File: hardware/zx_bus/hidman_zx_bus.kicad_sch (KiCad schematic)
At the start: 42 parts, among them J1 X1A, J1 ZX Keyboard, J2 GOTEK, J2 X1B, J3 UART, J4 USB_A, J5 USB_A, J6 Keyboard, J7 JTAG, J7 Mouse, J8 Kempston Mouse, J9 Z80, SW1 RESET, SW2 BOOT0, SW3 BOOT1, U1 CH559L, U2 EPM3128ATC100, U3 AMS1117-3.3, U4 74LVC1G125DB, Y1 12MHz

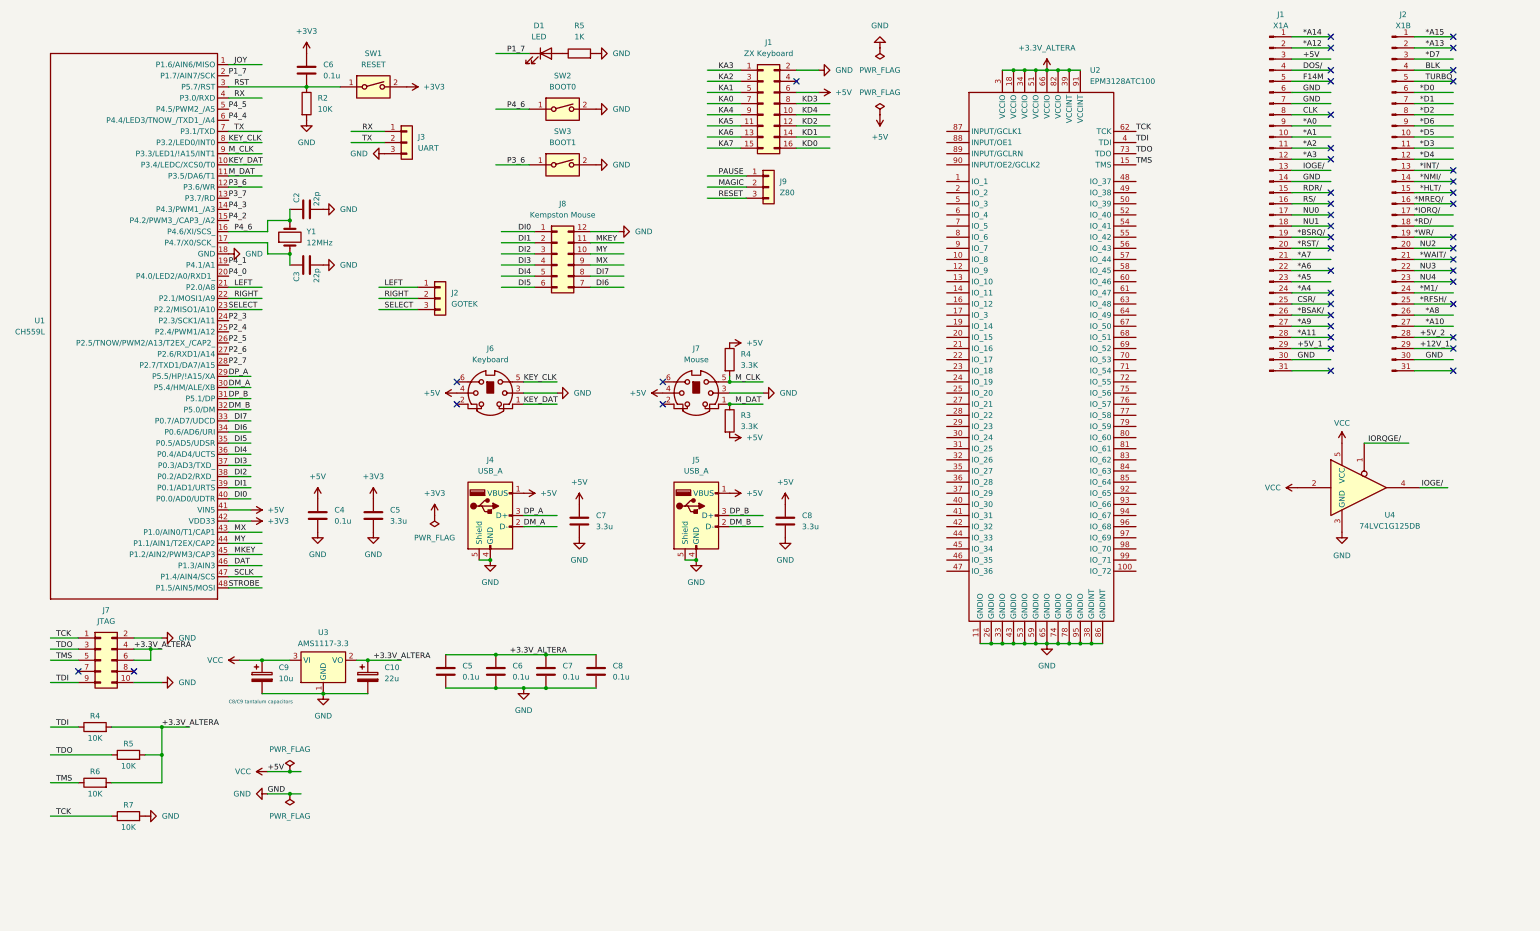
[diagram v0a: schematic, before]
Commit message: Route ZX BUS card PCB.
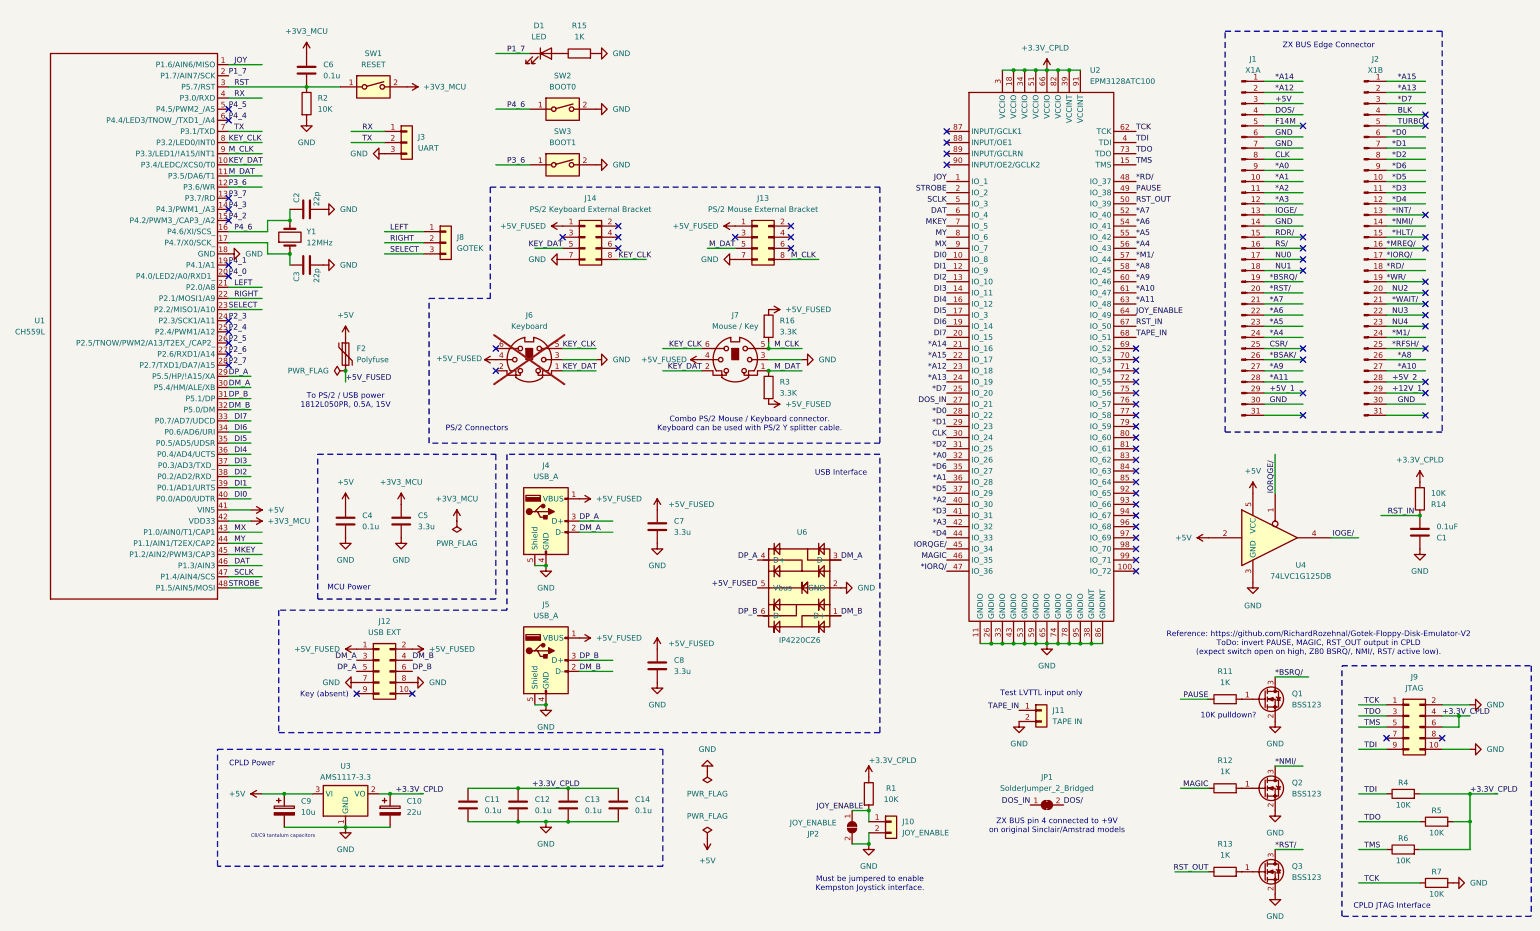
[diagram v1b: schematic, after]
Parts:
- removed J1: ZX Keyboard, Connector_PinHeader_2.54mm:PinHeader_2x08_P2.54mm_Vertical, symbol Connector_Generic:Conn_02x08_Odd_Even
- removed J8: Kempston Mouse, Connector_PinHeader_2.54mm:PinHeader_2x06_P2.54mm_Vertical, symbol Connector_Generic:Conn_02x06_Counter_Clockwise
- removed J9: Z80, Connector_PinHeader_2.54mm:PinHeader_1x03_P2.54mm_Vertical, symbol Connector_Generic:Conn_01x03
- added C1: 0.1uF, Capacitor_SMD:C_1206_3216Metric_Pad1.33x1.80mm_HandSolder, symbol Device:C
- added F2: Polyfuse, Fuse:Fuse_1812_4532Metric_Pad1.30x3.40mm_HandSolder, symbol Device:Polyfuse
- added J10: JOY_ENABLE, Connector_PinHeader_2.54mm:PinHeader_1x02_P2.54mm_Vertical, symbol Connector_Generic:Conn_01x02
- added J11: TAPE IN, Connector_PinHeader_2.54mm:PinHeader_1x02_P2.54mm_Vertical, symbol Connector_Generic:Conn_01x02
- added J12: USB EXT, Connector_PinHeader_2.54mm:PinHeader_2x05_P2.54mm_Vertical, symbol Connector_Generic:Conn_02x05_Odd_Even
- added J13: PS/2 Mouse External Bracket, Connector_PinHeader_2.54mm:PinHeader_2x04_P2.54mm_Vertical, symbol Connector_Generic:Conn_02x04_Odd_Even
- added J14: PS/2 Keyboard External Bracket, Connector_PinHeader_2.54mm:PinHeader_2x04_P2.54mm_Vertical, symbol Connector_Generic:Conn_02x04_Odd_Even
- added JP1: SolderJumper_2_Bridged, Jumper:SolderJumper-2_P1.3mm_Bridged_RoundedPad1.0x1.5mm, symbol Jumper:SolderJumper_2_Bridged
- added JP2: JOY_ENABLE, Jumper:SolderJumper-2_P1.3mm_Open_RoundedPad1.0x1.5mm, symbol Jumper:SolderJumper_2_Open
- added Q1, Q2, Q3: BSS123, Package_TO_SOT_SMD:SOT-23, symbol Transistor_FET:BSS123
- added R1, R14: 10K, Resistor_SMD:R_1206_3216Metric_Pad1.30x1.75mm_HandSolder, symbol Device:R
- added R11, R12, R13: 1K, Resistor_SMD:R_1206_3216Metric_Pad1.30x1.75mm_HandSolder, symbol Device:R
- added U6: IP4220CZ6, Package_SO:TSOP-6_1.65x3.05mm_P0.95mm, symbol IP4220CZ6:IP4220CZ6
- J4, J5: footprint Connector_USB:USB_A_Stewart_SS-52100-001_Horizontal -> Connector_USB:USB_A_Wuerth_614004134726_Horizontal
- J6: now not fitted; now left out of the parts list
- J7: value Mouse -> Mouse / Key
- renumbered C5 to C11, C6 to C12, C7 to C13, C8 to C14, J2 to J8, J7 to J9, R5 to R15, R4 to R16
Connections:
- net *A0: now also U2.32 (IO_26)
- net *A1: now also U2.36 (IO_28)
- net *A10: now also U2.61 (IO_47)
- net *A11: now also U2.63 (IO_48)
- net *A12: now also U2.23 (IO_18)
- net *A13: now also U2.24 (IO_19)
- net *A14: now also U2.21 (IO_16)
- net *A15: now also U2.22 (IO_17)
- net *A2: now also U2.40 (IO_30)
- net *A3: now also U2.42 (IO_32)
- net *A4: now also U2.56 (IO_43)
- net *A5: now also U2.55 (IO_42)
- net *A6: now also U2.54 (IO_41)
- net *A7: now also U2.52 (IO_40)
- net *A8: now also U2.58 (IO_45)
- net *A9: now also U2.60 (IO_46)
- net *BSRQ/: now also Q1.3 (D)
- net *D0: now also U2.28 (IO_22)
- net *D1: now also U2.29 (IO_23)
- net *D2: now also U2.31 (IO_25)
- net *D3: now also U2.41 (IO_31)
- net *D4: now also U2.44 (IO_33)
- net *D5: now also U2.37 (IO_29)
- net *D6: now also U2.35 (IO_27)
- net *D7: now also U2.25 (IO_20)
- net *IORQ/: now also U2.47 (IO_36)
- net *M1/: now also U2.57 (IO_44)
- net *NMI/: now also Q2.3 (D)
- net *RD/: now also U2.48 (IO_37)
- net *RST/: now also Q3.3 (D)
- net +5V: now also F2.1; no longer C7.1, C8.1, J4.1 (VBUS), J5.1 (VBUS), J6.4, J7.4, R16.1, R3.2
- net CLK: now also U2.30 (IO_24)
- net DAT: now also U2.6 (IO_4)
- net DI0: now also U2.10 (IO_8)
- net DI1: now also U2.12 (IO_9)
- net DI2: now also U2.13 (IO_10)
- net DI3: now also U2.14 (IO_11)
- net DI4: now also U2.16 (IO_12)
- net DI5: now also U2.17 (IO_3)
- net DI6: now also U2.19 (IO_14)
- net DI7: now also U2.20 (IO_15)
- net DM_A: now also J12.3 (Pin_3), U6.3 (D-)
- net DM_B: now also J12.4 (Pin_4), U6.1 (D+)
- net DOS/: now also JP1.2 (B)
- net DP_A: now also J12.5 (Pin_5), U6.4 (D+)
- net DP_B: now also J12.6 (Pin_6), U6.6 (D-)
- net GND: now also C1.1, J10.2 (Pin_2), J11.2 (Pin_2), J12.7 (Pin_7), J12.8 (Pin_8), J13.7 (Pin_7), J14.7 (Pin_7), JP2.2 (B), Q1.2 (S), Q2.2 (S), Q3.2 (S), U6.2 (GND)
- net IORQGE/: now also U2.45 (IO_34)
- net JOY: now also U2.1 (IO_1)
- net KEY_CLK: now also J7.6, J14.8 (Pin_8)
- net KEY_DAT: now also J7.2, J14.5 (Pin_5)
- net MAGIC: now also U2.46 (IO_35), R12.1
- net MKEY: now also U2.7 (IO_5)
- net MX: now also U2.9 (IO_7)
- net MY: now also U2.8 (IO_6)
- net M_CLK: now also J13.8 (Pin_8)
- net M_DAT: now also J13.5 (Pin_5)
- net PAUSE: now also U2.49 (IO_38), R11.1
- net SCLK: now also U2.5 (IO_3)
- net STROBE: now also U2.2 (IO_2)
- net DOS_IN: now reaches U2.27 (IO_21)
- net DOS_IN: now also JP1.1 (A)
- net RST_OUT: now reaches U2.50 (IO_39)
- net RST_OUT: now also R13.1
- net JOY_ENABLE: now reaches U2.64 (IO_49)
- net JOY_ENABLE: now also J10.1 (Pin_1), JP2.1 (A), R1.2
- net RST_IN: now reaches U2.67 (IO_50)
- net RST_IN: now also C1.2, R14.1
- net TAPE_IN: now reaches U2.68 (IO_51)
- net TAPE_IN: now also J11.1 (Pin_1)
- net +3.3V_ALTERA renamed +3.3V_CPLD
- net +3.3V_CPLD: now also R1.1, R14.2
- net +3V3 renamed +3V3_MCU
- new net: Q2.1 (G), R12.2
- new net: Q3.1 (G), R13.2
- new net: Q1.1 (G), R11.2
- new net +5V_FUSED: C7.1, C8.1, F2.2, J12.1 (Pin_1), J12.2 (Pin_2), J13.1 (Pin_1), J14.1 (Pin_1), J4.1 (VBUS), J5.1 (VBUS), J6.4, J7.4, R16.1, R3.2, U6.5 (Vbus)
- no-connect marks 45 -> 74
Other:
- note added: "10K pulldown?"
- note added: "CPLD JTAG Interface"
- note added: "CPLD Power"
- note added: "Combo PS/2 Mouse / Keyboard connector. Keyboard can be used with PS/2 Y splitter cable."
- note added: "Key (absent)"
- note added: "MCU Power"
- note added: "Must be jumpered to enable Kempston Joystick interface."
- note added: "PS/2 Connectors"
- note added: "Reference: https://github.com/RichardRozehnal/Gotek-Floppy-Disk-Emulator-V2 ToDo: invert PAUSE, MAGIC, RST_OUT output in CPLD (expect switch open on high, Z80 BSRQ/, NMI/, RST/ active low)."
- note added: "Test LVTTL input only"
- note added: "To PS/2 / USB power 1812L050PR, 0.5A, 15V"
- note added: "USB Interface"
- note added: "ZX BUS Edge Connector"
- note added: "ZX BUS pin 4 connected to +9V on original Sinclair/Amstrad models"
- moved on the sheet: C10, C11, C12, C13, C14, C4, C5, C7, C8, C9, J1, J2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

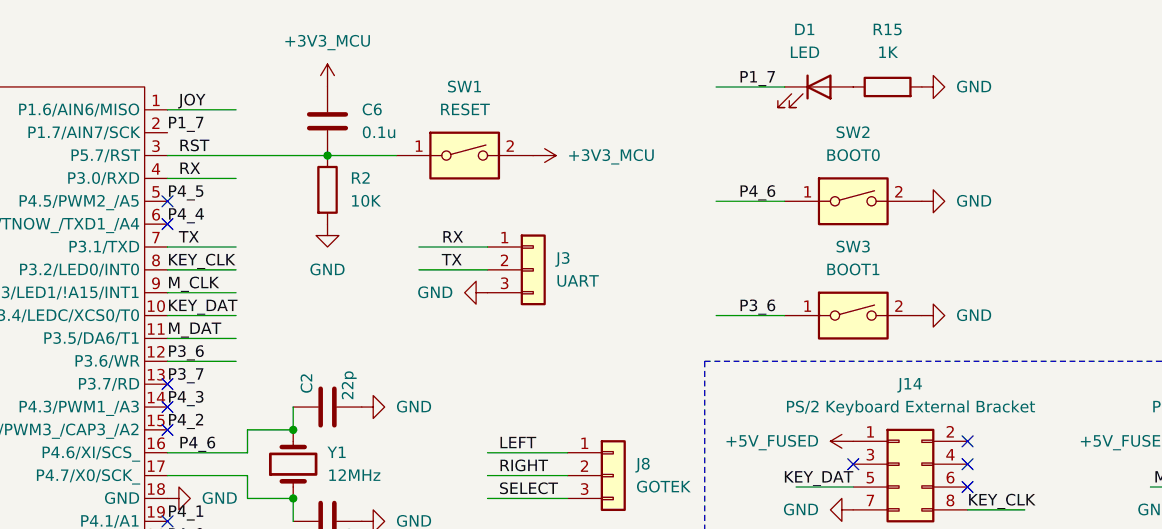
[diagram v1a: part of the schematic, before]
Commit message: Remove BOOT1 switch from schematic. Correct LED polarity.
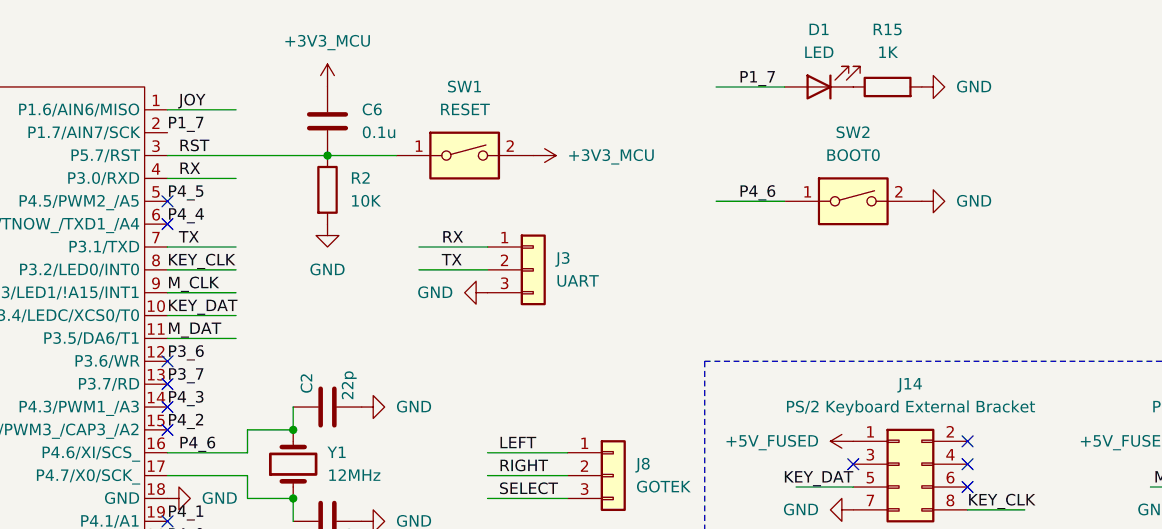
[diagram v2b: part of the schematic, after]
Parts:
- removed SW3: BOOT1, Connector_PinHeader_2.54mm:PinHeader_1x02_P2.54mm_Vertical, symbol Switch:SW_DIP_x01
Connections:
- net P1_7: now also D1.2 (A); no longer D1.1 (K)
- net at R15.1: now also D1.1 (K); no longer D1.2 (A)
- no-connect marks 74 -> 75
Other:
- moved on the sheet: D1
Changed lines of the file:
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@@
 	)
 	(no_connect
+		(at 63.5 50.8)
+	)
+	(no_connect
 		(at 270.51 118.11)
 	)
@@
 	(wire
 		(pts
-			(xy 63.5 50.8) (xy 71.12 50.8)
-		)
-		(stroke
-			(width 0)
-			(type default)
-		)
-	)
-	(wire
-		(pts
 			(xy 327.66 85.09) (xy 336.55 85.09)
 		)
@@
 	(wire
 		(pts
-			(xy 124.46 45.72) (xy 132.08 45.72)
-		)
-		(stroke
-			(width 0)
-			(type default)
-		)
-	)
-	(wire
-		(pts
 			(xy 327.66 92.71) (xy 336.55 92.71)
 		)
@@
 		)
 	)
-	(label "P3_6"
-		(at 127 45.72 0)
-		(fields_autoplaced yes)
-		(effects
-			(font
-				(size 1.27 1.27)
-			)
-			(justify left bottom)
-		)
-	)
 	(label "DOS{slash}"
 		(at 254 191.77 0)
@@
 	(symbol
 		(lib_id "power:GND")
-		(at 147.32 45.72 90)
-		(unit 1)
-		(exclude_from_sim no)
-		(in_bom yes)
-		(on_board yes)
-		(dnp no)
-		(fields_autoplaced yes)
-		(property "Reference" "#PWR034"
-			(at 153.67 45.72 0)
-			(effects
-				(font
-					(size 1.27 1.27)
-				)
-				(hide yes)
-			)
-		)
-		(property "Value" "GND"
-			(at 151.13 45.7199 90)
-			(effects
-				(font
-					(size 1.27 1.27)
-				)
-				(justify right)
-			)
-		)
-		(property "Footprint" ""
-			(at 147.32 45.72 0)
-			(effects
-				(font
-					(size 1.27 1.27)
-				)
-				(hide yes)
-			)
-		)
-		(property "Datasheet" ""
-			(at 147.32 45.72 0)
-			(effects
-				(font
-					(size 1.27 1.27)
-				)
-				(hide yes)
-			)
-		)
-		(property "Description" "Power symbol creates a global label with name \"GND\" , ground"
-			(at 147.32 45.72 0)
-			(effects
-				(font
-					(size 1.27 1.27)
-				)
-				(hide yes)
-			)
-		)
-		(pin "1"
-		)
-		(instances
-			(project "hidman_zx_bus"
-				(path "/3450efc4-f02c-4d95-a19b-bf60e75dcf1f"
-					(reference "#PWR034")
-					(unit 1)
-				)
-			)
-		)
-	)
-	(symbol
-		(lib_id "power:GND")
 		(at 147.32 20.32 90)
 		(unit 1)
@@
 	)
 	(symbol
-		(lib_id "Switch:SW_DIP_x01")
-		(at 139.7 45.72 0)
-		(unit 1)
-		(exclude_from_sim no)
-		(in_bom yes)
-		(on_board yes)
-		(dnp no)
-		(fields_autoplaced yes)
-		(property "Reference" "SW3"
-			(at 139.7 38.1 0)
-			(effects
-				(font
-					(size 1.27 1.27)
-				)
-			)
-		)
-		(property "Value" "BOOT1"
-			(at 139.7 40.64 0)
-			(effects
-				(font
-					(size 1.27 1.27)
-				)
-			)
-		)
-		(property "Footprint" "Connector_PinHeader_2.54mm:PinHeader_1x02_P2.54mm_Vertical"
-			(at 139.7 45.72 0)
-			(effects
-				(font
-					(size 1.27 1.27)
-				)
-				(hide yes)
-			)
-		)
-		(property "Datasheet" "~"
-			(at 139.7 45.72 0)
-			(effects
-				(font
-					(size 1.27 1.27)
-				)
-				(hide yes)
-			)
-		)
-		(property "Description" "1x DIP Switch, Single Pole Single Throw (SPST) switch, small symbol"
-			(at 139.7 45.72 0)
-			(effects
-				(font
-					(size 1.27 1.27)
-				)
-				(hide yes)
-			)
-		)
-		(pin "2"
-		)
-		(pin "1"
-		)
-		(instances
-			(project "hidman_zx_bus"
-				(path "/3450efc4-f02c-4d95-a19b-bf60e75dcf1f"
-					(reference "SW3")
-					(unit 1)
-				)
-			)
-		)
-	)
-	(symbol
 		(lib_id "power:GND")
 		(at 346.71 179.07 90)
@@
 	(symbol
 		(lib_id "Device:LED")
-		(at 135.89 20.32 0)
+		(at 135.89 20.32 180)
 		(unit 1)
 		(exclude_from_sim no)
@@
 		(on_board yes)
 		(dnp no)
-		(fields_autoplaced yes)
 		(property "Reference" "D1"
-			(at 134.3025 13.97 0)
+			(at 135.89 13.97 0)
 			(effects
 				(font
@@
 		)
 		(property "Value" "LED"
-			(at 134.3025 16.51 0)
+			(at 135.89 16.51 0)
 			(effects
 				(font
